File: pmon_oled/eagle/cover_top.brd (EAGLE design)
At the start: 66 x 66 mm, 1 part

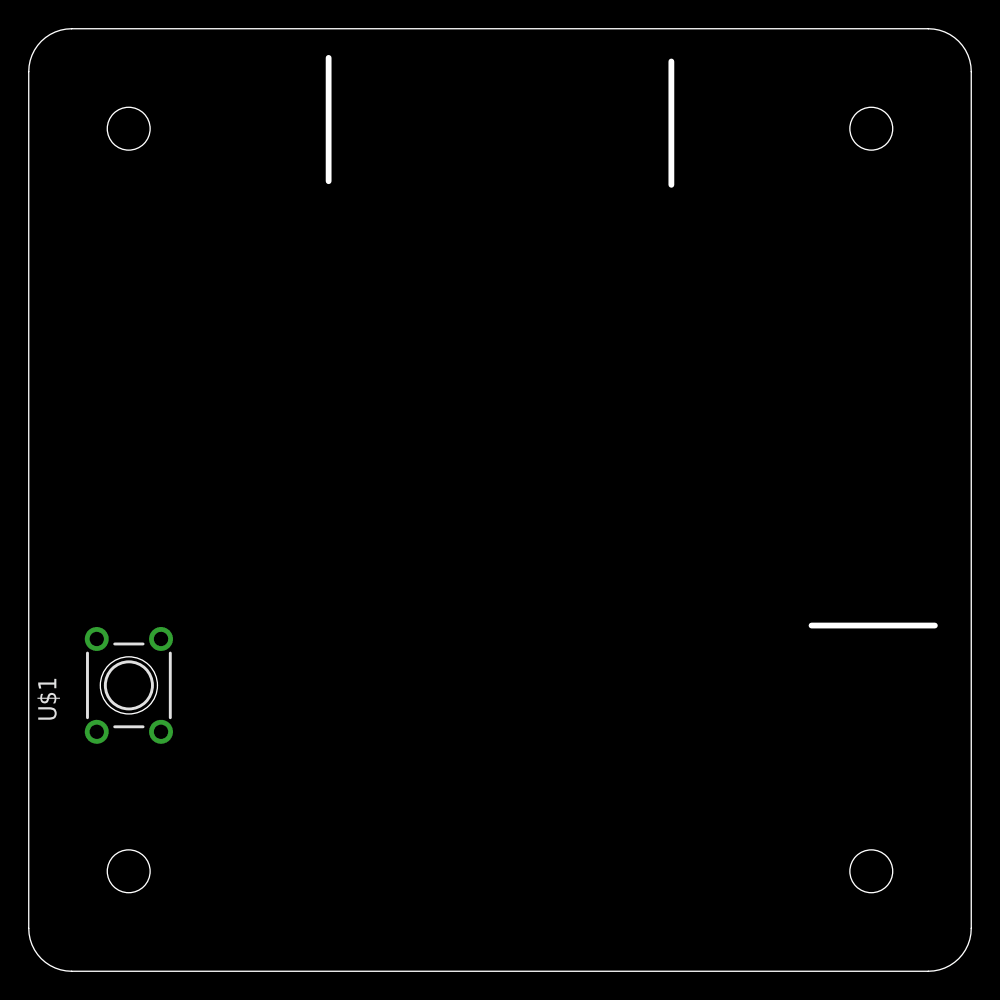
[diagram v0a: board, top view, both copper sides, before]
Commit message: Restoring the pmon_oled design with 3.8V regulator.
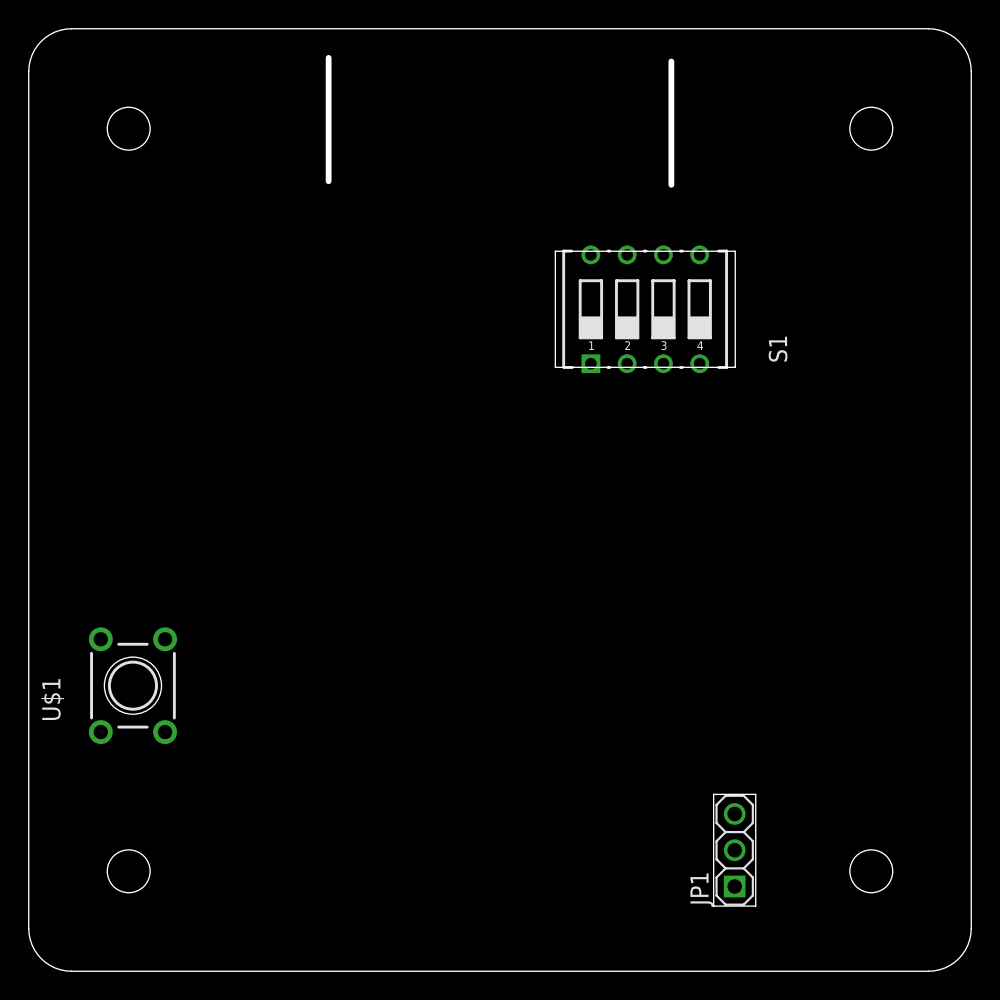
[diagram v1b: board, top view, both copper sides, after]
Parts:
- added JP1: (no value), pmon_oled:1X03
- added S1: DIP_SWITCH-X4, pmon_oled:DIP-SWITCH-X4
- moved U$1 0.29 mm to (4.30, 17.0)
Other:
- outline, holes or cut-outs redrawn
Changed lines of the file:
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@@
 <wire x1="60" y1="56" x2="56" y2="60" width="0" layer="48" style="shortdash" curve="90"/>
 <wire x1="56" y1="0" x2="60" y2="4" width="0" layer="48" style="shortdash" curve="90"/>
-<hole x="4.0132" y="17.018" drill="4"/>
+<hole x="4.2977375" y="16.99769375" drill="4"/>
+<wire x1="44.961809375" y1="1.56336875" x2="44.961809375" y2="9.38656875" width="0.0254" layer="20"/>
+<wire x1="44.961809375" y1="9.38656875" x2="47.908209375" y2="9.38656875" width="0.0254" layer="20"/>
+<wire x1="47.908209375" y1="9.38656875" x2="47.908209375" y2="1.56336875" width="0.0254" layer="20"/>
+<wire x1="47.908209375" y1="1.56336875" x2="44.961809375" y2="1.56336875" width="0.0254" layer="20"/>
+<wire x1="33.87598125" y1="39.29100625" x2="33.87598125" y2="47.41900625" width="0.0254" layer="20"/>
+<wire x1="33.87598125" y1="47.41900625" x2="46.47438125" y2="47.41900625" width="0.0254" layer="20"/>
+<wire x1="46.47438125" y1="47.41900625" x2="46.47438125" y2="39.29100625" width="0.0254" layer="20"/>
+<wire x1="46.47438125" y1="39.29100625" x2="33.87598125" y2="39.29100625" width="0.0254" layer="20"/>
 <wire x1="18" y1="52.324" x2="18" y2="60.96" width="0.4064" layer="20"/>
 <wire x1="42" y1="52.07" x2="42" y2="60.706" width="0.4064" layer="20"/>
-<wire x1="60.452" y1="21.209" x2="51.816" y2="21.209" width="0.4064" layer="20"/>
 </plain>
 <attributes>
@@
 </autorouter>
 <elements>
-<element name="U$1" library="pmon_oled" package="TLE1105" value="PUSH_BUTTON" x="4.0132" y="17.018"/>
+<element name="S1" library="pmon_oled" package="DIP-SWITCH-X4" value="DIP_SWITCH-X4" x="36.365" y="39.545"/>
+<element name="JP1" library="pmon_oled" package="1X03" value="" x="46.435" y="5.475" rot="R90"/>
+<element name="U$1" library="pmon_oled" package="TLE1105" value="PUSH_BUTTON" x="4.2977375" y="16.99769375"/>
 </elements>
 <signals>

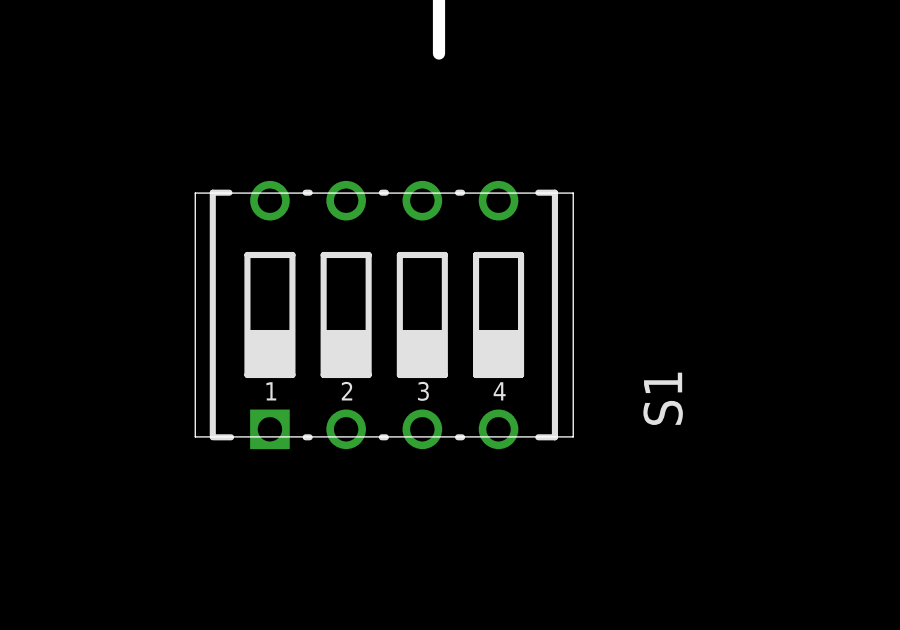
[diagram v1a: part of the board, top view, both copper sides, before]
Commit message: Removed the config dip switches.
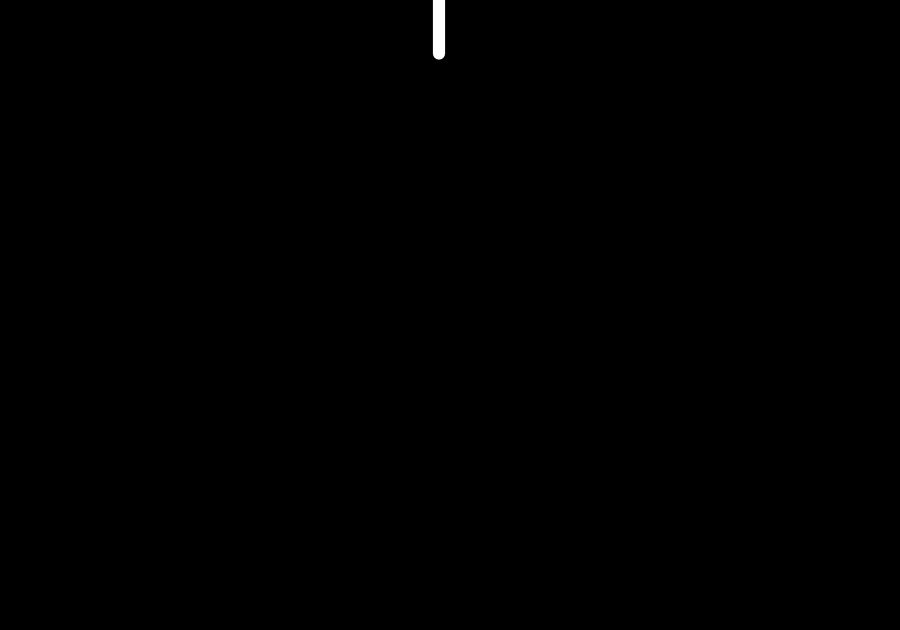
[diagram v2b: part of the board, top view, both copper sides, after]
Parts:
- removed S1: DIP_SWITCH-X4, pmon_oled:DIP-SWITCH-X4
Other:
- outline, holes or cut-outs redrawn
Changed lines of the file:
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@@
 <wire x1="47.908209375" y1="9.38656875" x2="47.908209375" y2="1.56336875" width="0.0254" layer="20"/>
 <wire x1="47.908209375" y1="1.56336875" x2="44.961809375" y2="1.56336875" width="0.0254" layer="20"/>
-<wire x1="33.87598125" y1="39.29100625" x2="33.87598125" y2="47.41900625" width="0.0254" layer="20"/>
-<wire x1="33.87598125" y1="47.41900625" x2="46.47438125" y2="47.41900625" width="0.0254" layer="20"/>
-<wire x1="46.47438125" y1="47.41900625" x2="46.47438125" y2="39.29100625" width="0.0254" layer="20"/>
-<wire x1="46.47438125" y1="39.29100625" x2="33.87598125" y2="39.29100625" width="0.0254" layer="20"/>
 <wire x1="18" y1="52.324" x2="18" y2="60.96" width="0.4064" layer="20"/>
 <wire x1="42" y1="52.07" x2="42" y2="60.706" width="0.4064" layer="20"/>
@@
 </autorouter>
 <elements>
-<element name="S1" library="pmon_oled" package="DIP-SWITCH-X4" value="DIP_SWITCH-X4" x="36.365" y="39.545"/>
 <element name="JP1" library="pmon_oled" package="1X03" value="" x="46.435" y="5.475" rot="R90"/>
 <element name="U$1" library="pmon_oled" package="TLE1105" value="PUSH_BUTTON" x="4.2977375" y="16.99769375"/>
